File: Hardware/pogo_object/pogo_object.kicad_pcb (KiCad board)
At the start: 2 copper layers, 124 x 124 mm, 33 parts, among them J1 10132797-035100LF, J2 10132797-015100LF, J3 Conn_01x02_Male, J4 Conn_01x02_Male, J5 Conn_01x04_Male, U2 BSR802NL6327HTSA1, U3 mcp1407, U4 BSR802NL6327HTSA1

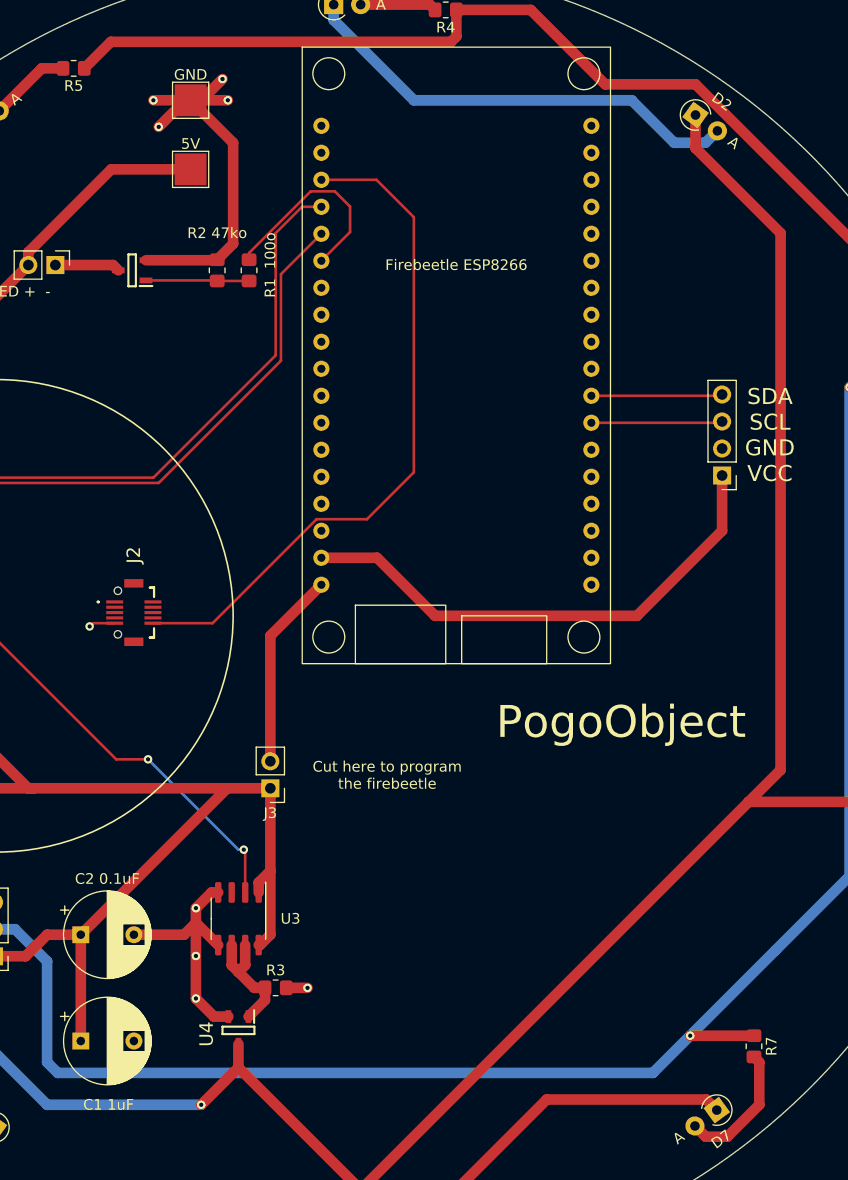
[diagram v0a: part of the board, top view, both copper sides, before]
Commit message: adding battery voltage monitoring
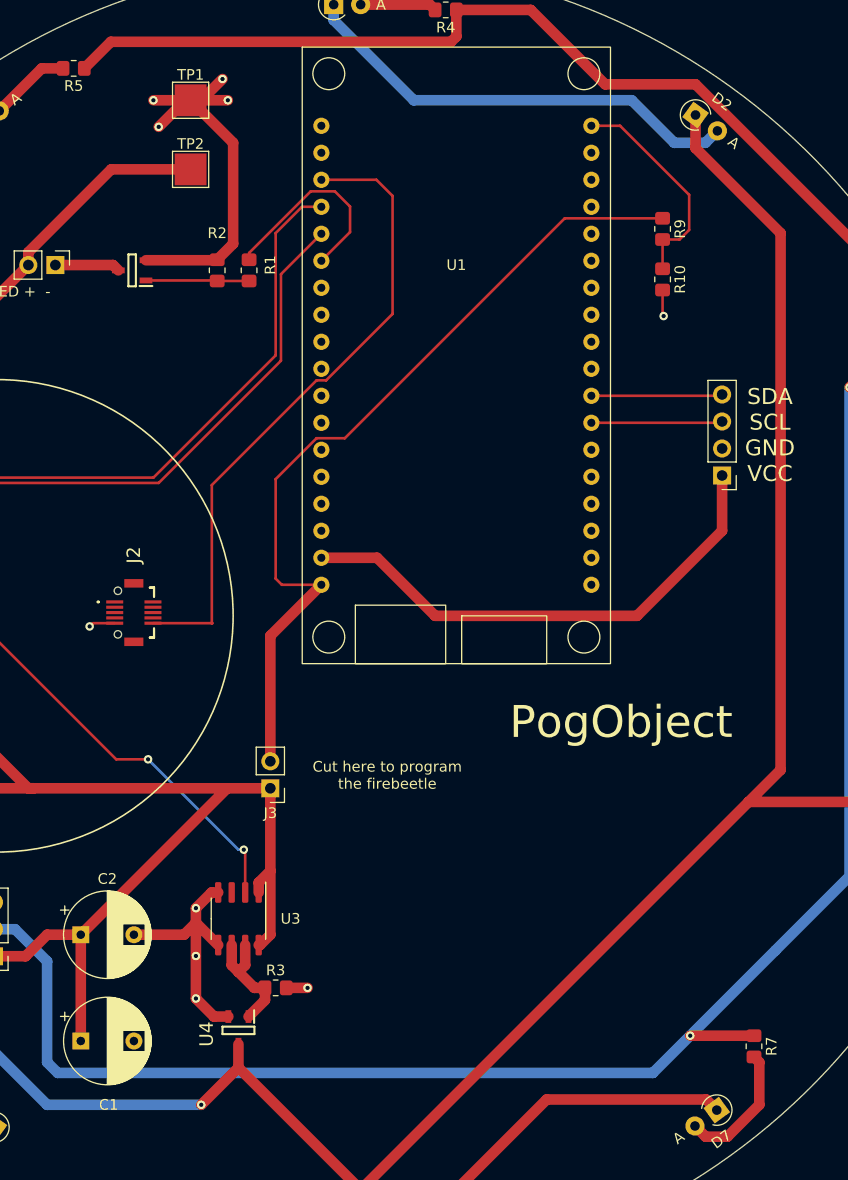
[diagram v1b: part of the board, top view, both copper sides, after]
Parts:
- added R10: 100k, Resistor_SMD:R_0805_2012Metric_Pad1.20x1.40mm_HandSolder, F.Cu at (149.9, 77.8)
- added R9: 100k, Resistor_SMD:R_0805_2012Metric_Pad1.20x1.40mm_HandSolder, F.Cu at (149.9, 73.1)
- C1: renamed from C1 1uF
- C2: renamed from C2 0.1uF
- R1: renamed from R1  100o
- R2: renamed from R2 47ko
- U1: renamed from Firebeetle ESP8266
- renumbered GND to TP1, 5V to TP2
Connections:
- net Net-(J3-Pad2) renamed VBAT
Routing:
- net VBAT: track 18.6 -> 79.1 mm
- net unconnected-(U1-Pad36): track 0.00 -> 20.8 mm
- net ~{RESET}: track 64.6 -> 60.7 mm
- net GND: track 80.4 -> 82.8 mm, vias 12 -> 13
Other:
- board text added: "PogObject"
- board text removed: "PogoObject"

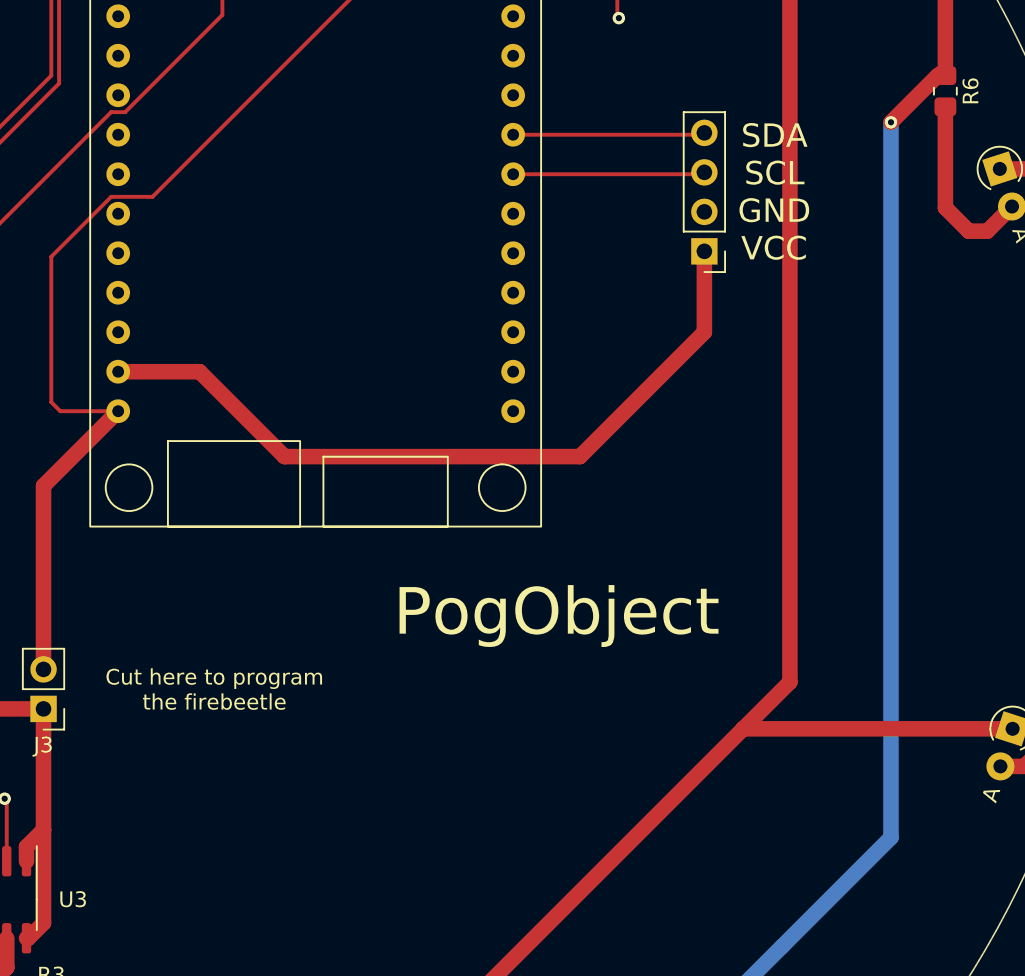
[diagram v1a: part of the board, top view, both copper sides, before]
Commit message: updates the pogobject pcb to include config mode
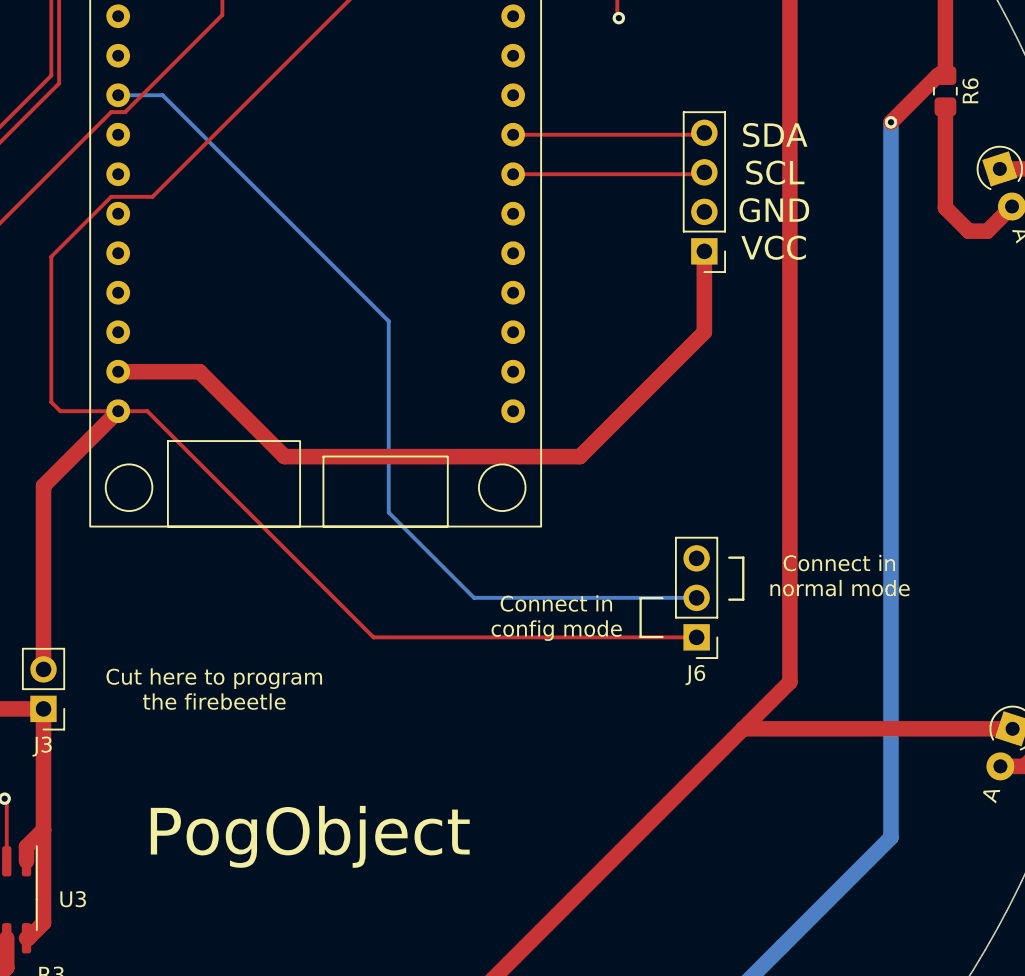
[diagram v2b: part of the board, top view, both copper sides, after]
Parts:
- added J6: Conn_01x03_Male, Connector_PinHeader_2.54mm:PinHeader_1x03_P2.54mm_Vertical, F.Cu at (155.0, 121.1)
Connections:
- U1 pad 10: unconnected-(U1-Pad10) -> Net-(U1-Pad10)
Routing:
- net Net-(U1-Pad10): track 0.00 -> 57.8 mm
- net VBAT: track 79.1 -> 122.3 mm
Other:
- board text added: "Connect in config mode"
- board text added: "Connect in normal mode"
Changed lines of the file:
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@@
   (net 63 "unconnected-(U1-Pad8)")
   (net 64 "unconnected-(U1-Pad9)")
-  (net 65 "unconnected-(U1-Pad10)")
+  (net 65 "Net-(U1-Pad10)")
   (net 66 "unconnected-(U1-Pad11)")
   (net 67 "unconnected-(U1-Pad12)")
@@
   (net 84 "unconnected-(U1-Pad34)")
   (net 85 "unconnected-(U1-Pad35)")
-  (net 86 "unconnected-(U1-Pad36)")
+  (net 86 "unconnected-(R10-Pad1)")
   (net 87 "unconnected-(U3-Pad3)")
   (footprint "Capacitor_THT:CP_Radial_D8.0mm_P5.00mm" (layer "F.Cu")
@@
       (net 64 "unconnected-(U1-Pad9)") (pinfunction "D8") (pintype "bidirectional+no_connect"))
     (pad "10" thru_hole circle (at -12.7 1.26) (size 1.524 1.524) (drill 0.762) (layers *.Cu *.Mask)
-      (net 65 "unconnected-(U1-Pad10)") (pinfunction "D9") (pintype "bidirectional+no_connect"))
+      (net 65 "Net-(U1-Pad10)") (pinfunction "D9") (pintype "bidirectional"))
     (pad "11" thru_hole circle (at -12.7 3.8) (size 1.524 1.524) (drill 0.762) (layers *.Cu *.Mask)
       (net 66 "unconnected-(U1-Pad11)") (pinfunction "NC") (pintype "no_connect"))
@@
       (net 85 "unconnected-(U1-Pad35)") (pinfunction "NC") (pintype "no_connect"))
     (pad "36" thru_hole circle (at 12.7 -21.6) (size 1.524 1.524) (drill 0.762) (layers *.Cu *.Mask)
-      (net 86 "unconnected-(U1-Pad36)") (pinfunction "A0") (pintype "input+no_connect"))
+      (net 86 "unconnected-(R10-Pad1)") (pinfunction "A0") (pintype "input+no_connect"))
   )
   (footprint "Resistor_SMD:R_0805_2012Metric_Pad1.20x1.40mm_HandSolder" (layer "F.Cu")
@@
     (fp_line (start -1 0.625) (end -1 -0.625) (layer "F.Fab") (width 0.1))
     (pad "1" smd roundrect (at -1 0 270) (size 1.2 1.4) (layers "F.Cu" "F.Paste" "F.Mask") (roundrect_rratio 0.208333)
-      (net 86 "unconnected-(U1-Pad36)") (pintype "passive+no_connect"))
+      (net 86 "unconnected-(R10-Pad1)") (pintype "passive+no_connect"))
     (pad "2" smd roundrect (at 1 0 270) (size 1.2 1.4) (layers "F.Cu" "F.Paste" "F.Mask") (roundrect_rratio 0.208333)
       (net 1 "GND") (pintype "passive"))
@@
     )
   )
+  (footprint "Connector_PinHeader_2.54mm:PinHeader_1x03_P2.54mm_Vertical" (layer "F.Cu")
+    (at 155 121.125 180)
+    (descr "Through hole straight pin header, 1x03, 2.54mm pitch, single row")
+    (tags "Through hole pin header THT 1x03 2.54mm single row")
+    (property "Sheetfile" "pogo_object.kicad_sch")
+    (property "Sheetname" "")
+    (attr through_hole)
+    (fp_text reference "J6" (at 0 -2.33) (layer "F.SilkS")
+      (effects (font (size 1 1) (thickness 0.15)))
+    )
+    (fp_text value "Conn_01x03_Male" (at 0 7.41) (layer "F.Fab")
+      (effects (font (size 1 1) (thickness 0.15)))
+    )
+    (fp_text user "${REFERENCE}" (at 0 2.54 90) (layer "F.Fab")
+      (effects (font (size 1 1) (thickness 0.15)))
+    )
+    (fp_line (start -1.33 -1.33) (end 0 -1.33) (layer "F.SilkS") (width 0.12))
+    (fp_line (start -1.33 6.41) (end 1.33 6.41) (layer "F.SilkS") (width 0.12))
+    (fp_line (start -1.33 1.27) (end 1.33 1.27) (layer "F.SilkS") (width 0.12))
+    (fp_line (start -1.33 1.27) (end -1.33 6.41) (layer "F.SilkS") (width 0.12))
+    (fp_line (start 1.33 1.27) (end 1.33 6.41) (layer "F.SilkS") (width 0.12))
+    (fp_line (start -1.33 0) (end -1.33 -1.33) (layer "F.SilkS") (width 0.12))
+    (fp_line (start -1.8 -1.8) (end -1.8 6.85) (layer "F.CrtYd") (width 0.05))
+    (fp_line (start 1.8 6.85) (end 1.8 -1.8) (layer "F.CrtYd") (width 0.05))
+    (fp_line (start -1.8 6.85) (end 1.8 6.85) (layer "F.CrtYd") (width 0.05))
+    (fp_line (start 1.8 -1.8) (end -1.8 -1.8) (layer "F.CrtYd") (width 0.05))
+    (fp_line (start -1.27 -0.635) (end -0.635 -1.27) (layer "F.Fab") (width 0.1))
+    (fp_line (start 1.27 6.35) (end -1.27 6.35) (layer "F.Fab") (width 0.1))
+    (fp_line (start 1.27 -1.27) (end 1.27 6.35) (layer "F.Fab") (width 0.1))
+    (fp_line (start -1.27 6.35) (end -1.27 -0.635) (layer "F.Fab") (width 0.1))
+    (fp_line (start -0.635 -1.27) (end 1.27 -1.27) (layer "F.Fab") (width 0.1))
+    (pad "1" thru_hole rect (at 0 0 180) (size 1.7 1.7) (drill 1) (layers *.Cu *.Mask)
+      (net 50 "VBAT") (pinfunction "Pin_1") (pintype "passive"))
+    (pad "2" thru_hole oval (at 0 2.54 180) (size 1.7 1.7) (drill 1) (layers *.Cu *.Mask)
+      (net 65 "Net-(U1-Pad10)") (pinfunction "Pin_2") (pintype "passive"))
+    (pad "3" thru_hole oval (at 0 5.08 180) (size 1.7 1.7) (drill 1) (layers *.Cu *.Mask)
+      (net 1 "GND") (pinfunction "Pin_3") (pintype "passive"))
+    (model "${KICAD6_3DMODEL_DIR}/Connector_PinHeader_2.54mm.3dshapes/PinHeader_1x03_P2.54mm_Vertical.wrl"
+      (offset (xyz 0 0 0))
+      (scale (xyz 1 1 1))
+      (rotate (xyz 0 0 0))
+    )
+  )
   (footprint "Resistor_SMD:R_0805_2012Metric_Pad1.20x1.40mm_HandSolder" (layer "F.Cu")
     (at 84 149.5 -90)
@@
       (net 50 "VBAT") (pintype "passive"))
     (pad "2" smd roundrect (at 1 0 270) (size 1.2 1.4) (layers "F.Cu" "F.Paste" "F.Mask") (roundrect_rratio 0.208333)
-      (net 86 "unconnected-(U1-Pad36)") (pintype "passive+no_connect"))
+      (net 86 "unconnected-(R10-Pad1)") (pintype "passive+no_connect"))
     (model "${KICAD6_3DMODEL_DIR}/Resistor_SMD.3dshapes/R_0805_2012Metric.wrl"
       (offset (xyz 0 0 0))
@@
       ) (layer "B.SilkS") (width 0.01) (fill solid))
   )
+  (gr_line (start 151.4 121.1) (end 152.8 121.1) (layer "F.SilkS") (width 0.15))
+  (gr_line (start 158 118.7) (end 157.1 118.7) (layer "F.SilkS") (width 0.15))
+  (gr_line (start 152.8 118.6) (end 151.4 118.6) (layer "F.SilkS") (width 0.15))
+  (gr_line (start 158 116) (end 158 118.7) (layer "F.SilkS") (width 0.15))
+  (gr_line (start 157.1 116) (end 158 116) (layer "F.SilkS") (width 0.15))
+  (gr_line (start 151.4 118.6) (end 151.4 121.1) (layer "F.SilkS") (width 0.15))
   (gr_circle (center 87.275 109.5) (end 87.275 87.275) (layer "F.SilkS") (width 0.15) (fill none))
   (gr_circle (center 120 110) (end 182 110) (layer "Edge.Cuts") (width 0.1) (fill none))
@@
     (effects (font (size 1 1) (thickness 0.15)))
   )
-  (gr_text "PogObject" (at 146 119.5) (layer "F.SilkS")
+  (gr_text "Connect in \nnormal mode" (at 164.2 117.2) (layer "F.SilkS")
+    (effects (font (size 1 1) (thickness 0.15)))
+  )
+  (gr_text "PogObject" (at 130 133.7) (layer "F.SilkS")
     (effects (font (size 3 3) (thickness 0.75)))
   )
@@
     (effects (font (size 1 1) (thickness 0.15)))
   )
+  (gr_text "Connect in \nconfig mode" (at 146 119.8) (layer "F.SilkS")
+    (effects (font (size 1 1) (thickness 0.15)))
+  )
   (gr_text "R var" (at 84 140.5 90) (layer "F.SilkS")
     (effects (font (size 1 1) (thickness 0.15)))
@@
   (segment (start 113.5 96.642749) (end 113.5 106) (width 0.25) (layer "F.Cu") (net 50))
   (segment (start 117.8 106.58) (end 113 111.38) (width 1) (layer "F.Cu") (net 50))
+  (segment (start 117.8 106.58) (end 119.68 106.58) (width 0.25) (layer "F.Cu") (net 50))
   (segment (start 120.007 92.793) (end 117.349749 92.793) (width 0.25) (layer "F.Cu") (net 50))
+  (segment (start 119.68 106.58) (end 134.225 121.125) (width 0.25) (layer "F.Cu") (net 50))
   (segment (start 149.893 72.107) (end 140.693 72.107) (width 0.25) (layer "F.Cu") (net 50))
   (segment (start 113.5 106) (end 114.08 106.58) (width 0.25) (layer "F.Cu") (net 50))
@@
   (segment (start 117.349749 92.793) (end 113.5 96.642749) (width 0.25) (layer "F.Cu") (net 50))
   (segment (start 149.9 72.1) (end 149.893 72.107) (width 0.25) (layer "F.Cu") (net 50))
+  (segment (start 134.225 121.125) (end 155 121.125) (width 0.25) (layer "F.Cu") (net 50))
   (segment (start 98.2 76.5) (end 98.7 77) (width 1) (layer "F.Cu") (net 51))
   (segment (start 92.775 76.5) (end 98.2 76.5) (width 1) (layer "F.Cu") (net 51))
@@
   (segment (start 92 151.5) (end 93 152.5) (width 1) (layer "B.Cu") (net 58))
   (segment (start 152.5 149) (end 160.5 141) (width 1) (layer "B.Cu") (net 58))
+  (segment (start 117.8 86.26) (end 120.66 86.26) (width 0.25) (layer "B.Cu") (net 65))
+  (segment (start 135.2 100.8) (end 135.2 113.1) (width 0.25) (layer "B.Cu") (net 65))
+  (segment (start 135.2 113.1) (end 140.685 118.585) (width 0.25) (layer "B.Cu") (net 65))
+  (segment (start 120.66 86.26) (end 135.2 100.8) (width 0.25) (layer "B.Cu") (net 65))
+  (segment (start 140.685 118.585) (end 155 118.585) (width 0.25) (layer "B.Cu") (net 65))
   (segment (start 152.4 69.9) (end 152.4 73.2) (width 0.25) (layer "F.Cu") (net 86))
   (segment (start 143.2 63.4) (end 145.9 63.4) (width 0.25) (layer "F.Cu") (net 86))
